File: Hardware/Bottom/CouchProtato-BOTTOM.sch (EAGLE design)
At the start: 44 parts, among them U1 AD5242-SO16, U4 PCF8523

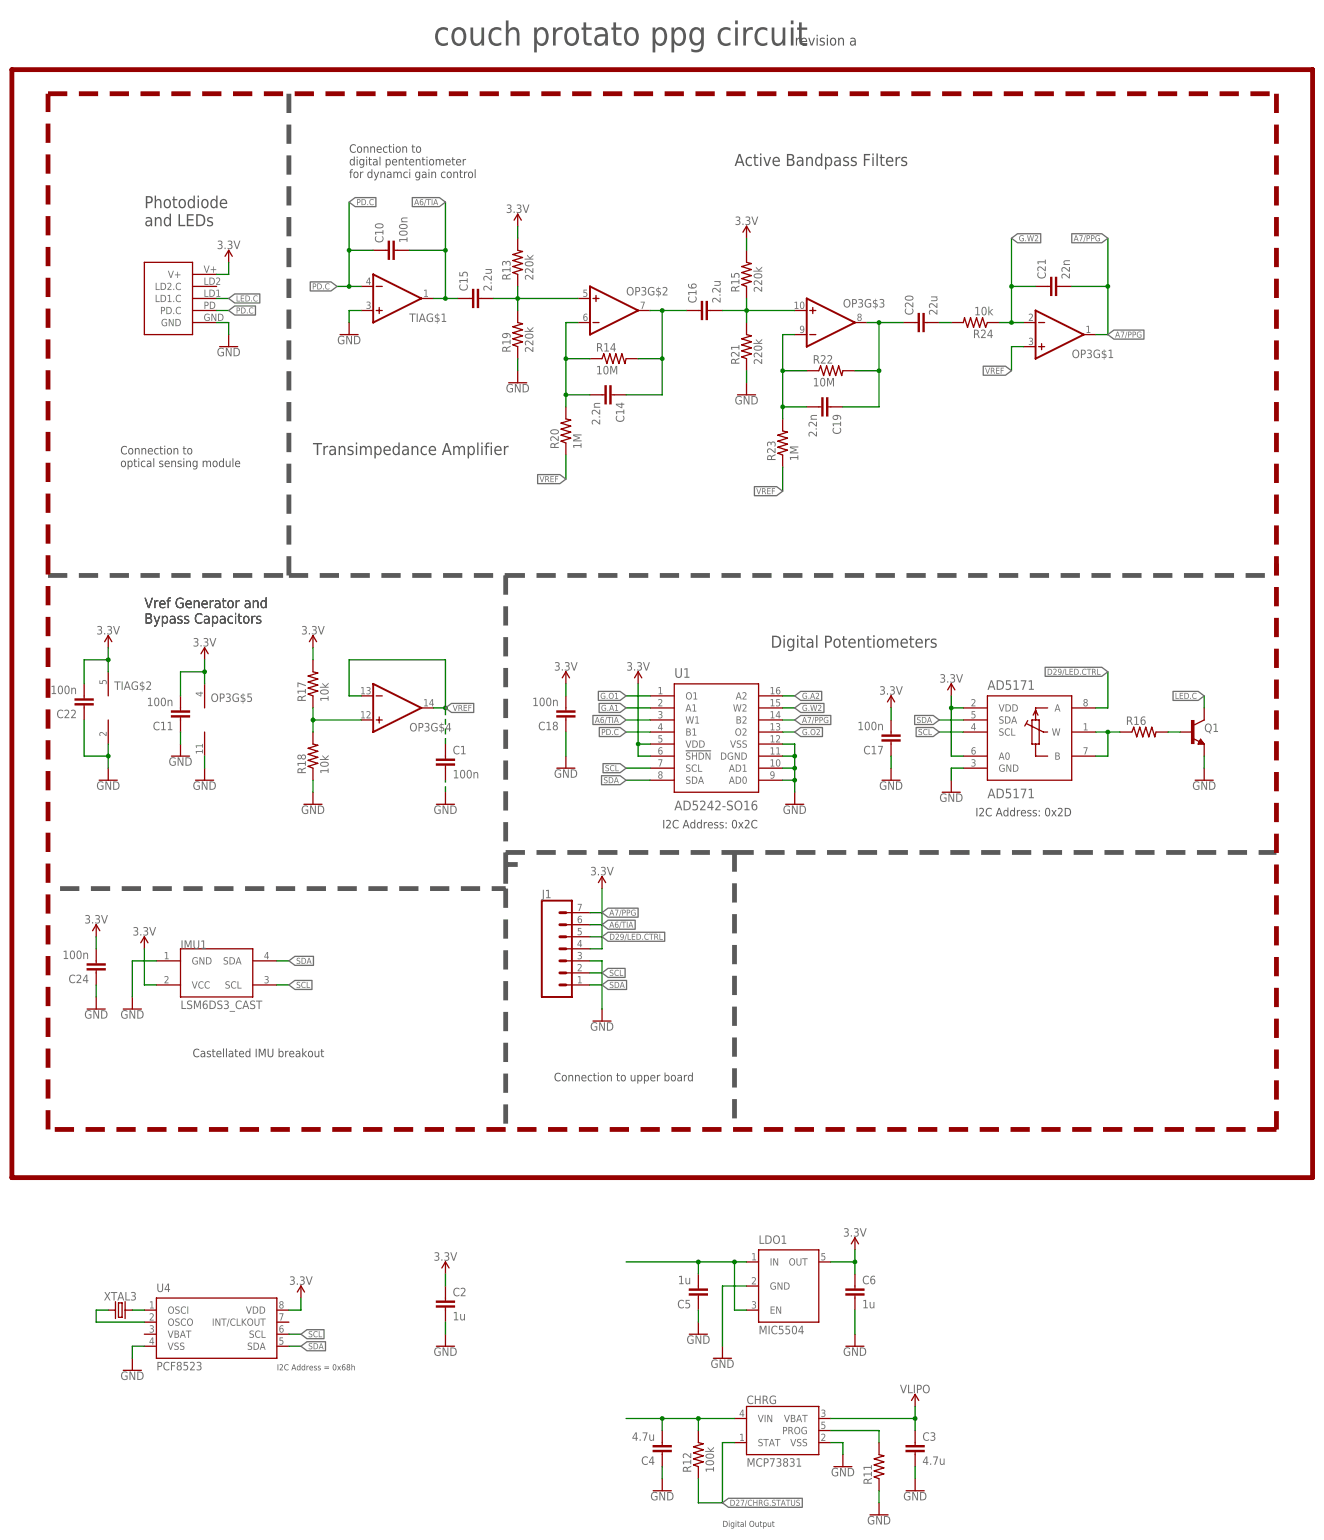
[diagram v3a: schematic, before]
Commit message: Finished first revisions of EAGLE designs for smartwatch
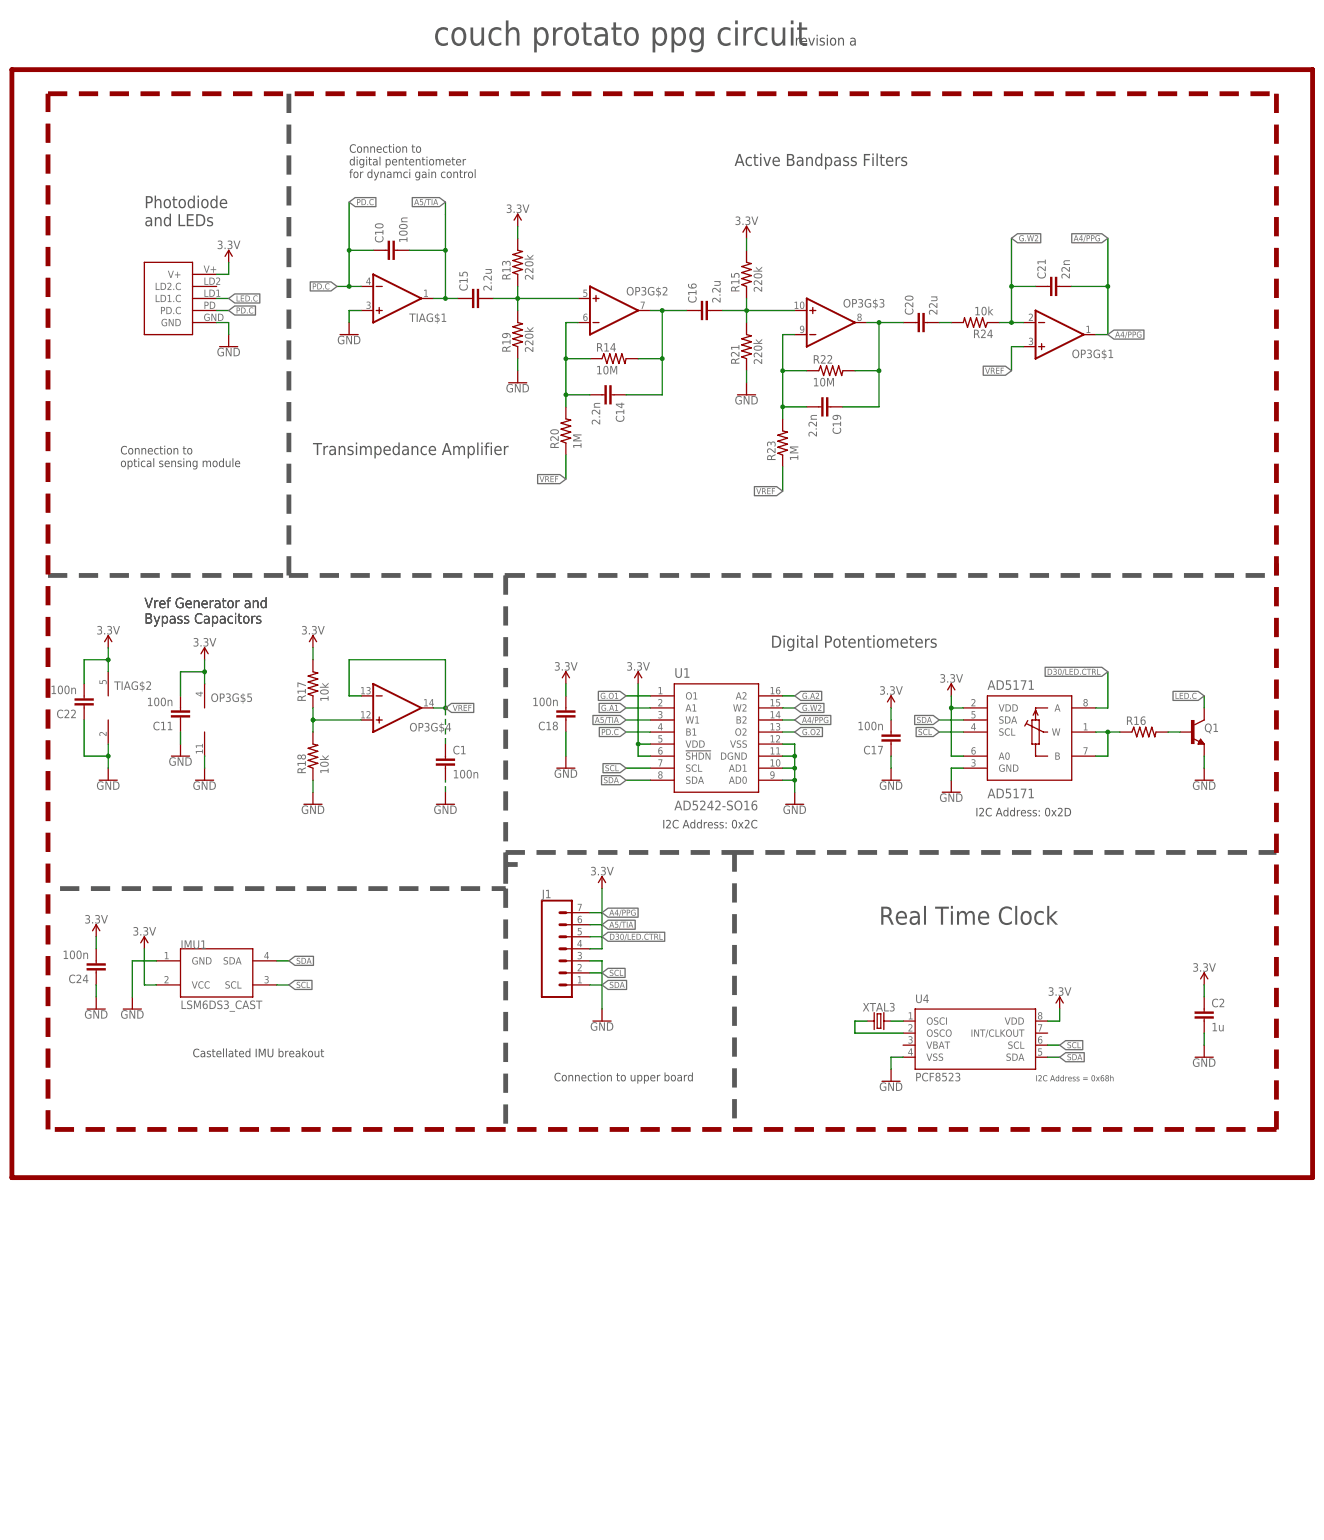
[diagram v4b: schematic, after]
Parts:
- removed C3, C4: 4.7u, LinnesLab-Passives:CAPACITOR0603
- removed C5, C6: 1u, LinnesLab-Passives:CAPACITOR0603
- removed CHRG: MCP73831, LinnesLab-Power:MCP73831
- removed LDO1: MIC5504, LinnesLab-Power:MIC5504
- removed R11: (no value), LinnesLab-Passives:RESISTOR0603
- removed R12: 100k, LinnesLab-Passives:RESISTOR0603
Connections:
- net A6/TIA renamed A5/TIA
- net A7/PPG renamed A4/PPG
- net D29/LED.CTRL renamed D30/LED.CTRL
- removed net D27/CHRG.STATUS: CHRG.STAT, R12.1
- removed net N$3: CHRG.PROG, R11.2
- removed net VIN1: C4.2, C5.2, CHRG.VIN, LDO1.EN, LDO1.IN, R12.2
- removed net VLIPO: C3.1, CHRG.VBAT
- net 3.3V: no longer C6.1, LDO1.OUT
- net GND: no longer C3.2, C4.1, C5.1, C6.2, CHRG.VSS, LDO1.GND, R11.1
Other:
- note added: "Real Time Clock"
- note removed: "Digital Output"
- moved on the sheet: C2, U4, XTAL3
